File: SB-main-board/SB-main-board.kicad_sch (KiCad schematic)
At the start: 95 parts, among them J1 XT30PB_IN, J2 USB_C_Receptacle_USB2.0_16P, J3 Excluder, J4 PT100, J5 Hotend, J6 FAN2, J7 LDC, J8 FS, J9 FAN, Q1 BUK9M8R5-40EX, SW1 BOOT, U1 RP2040, U10 TMP235A2, U11 LP5912-3.3DRV, U2 W25Q16JVUXIQ, U3 TJA1042TK-3, U4 TPS54302, U5 LP5912-3.3DRV, U6 TMC2208-LA, U7 OR, U8 ADXL343, U9 MAX31865xTP, Y1 12MHz

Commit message: update to v2
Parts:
- removed C36: 1uF, Capacitor_SMD:C_0603_1608Metric, symbol Device:C_Small
- removed C37: 47pF, Capacitor_SMD:C_0402_1005Metric, symbol Device:C_Small
- removed FB1, FB2, FB3, FB4, FB6: 120R@100MHz, Inductor_SMD:L_0603_1608Metric, symbol Device:FerriteBead
- removed U11: LP5912-3.3DRV, Package_SON:WSON-6-1EP_2x2mm_P0.65mm_EP1x1.6mm, symbol Regulator_Linear:LP5912-3.3DRV
- removed U4: TPS54302, Package_TO_SOT_SMD:SOT-23-6, symbol Regulator_Switching:TPS565208
- removed U6: TMC2208-LA, Package_DFN_QFN:QFN-28-1EP_5x5mm_P0.5mm_EP3.75x3.75mm, symbol Driver_Motor:TMC2208-LA
- added D3: TPD4E02B04DQA, Package_SON:USON-10_2.5x1.0mm_P0.5mm, symbol Power_Protection:TPD4E02B04DQA
- added U4: TPS560430YF, Package_TO_SOT_SMD:SOT-23-6, symbol Library:TPS560430YF
- added U6: TMC2208-LA, Package_DFN_QFN:QFN-28-1EP_5x5mm_P0.5mm_EP3.75x3.75mm, symbol Library:TMC2208-LA
- C16: value 10uF -> 2.2uF
- C35: value 2.2uF -> 100nF; footprint Capacitor_SMD:C_0603_1608Metric -> Capacitor_SMD:C_0402_1005Metric
- D2: renamed from D3; value D_Schottky -> Schottky
- L1: footprint Inductor_SMD:L_Sunlord_SWPA4030S -> Library:L_Changjiang_FTC303020D
- R11: now fitted
- R12: value 100K -> 88.7K
- R13: value 13.3K -> 22.1K
- R7: footprint Resistor_SMD:R_0402_1005Metric -> Resistor_SMD:R_0805_2012Metric
- SW1: symbol Switch:SW_SPST -> Switch:SW_Push_Dual_x2
- U7: footprint Package_TO_SOT_SMD:SOT-23-5 -> Package_TO_SOT_SMD:SOT-353_SC-70-5
- renumbered C19 to C17, C17 to C18, C18 to C19, D2 to D4, FB5 to FB1
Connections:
- net +3V3B is gone; now on net +3V3: C20.1, C21.1, C29.1, C30.1, C31.1, C32.1, FB1.1, J8.4 (Pin_4), J9.8 (Pin_8), R14.1, U7.5 (VCC), U8.1 (Vdd_I/O), U8.6 (Vs), U9.19 (DVDD)
- net PGND is gone; now on net GND: C16.2, C18.2, C22.2, C23.2, C24.2, C27.2, C28.2, H1.1, H2.1, J1.2 (Pin_2), J3.MP (MountPin), J6.MP (MountPin), J7.MP (MountPin), J8.MP (MountPin), J9.10 (Pin_10), J9.12 (Pin_12), Q1.1 (S), Q1.2 (S), Q1.3 (S), R13.2, R15.2, R16.2, R20.2
- net +24V: now also C35.1, U4.5 (VIN), U6.22 (VS), U6.28 (VS)
- net +5V: no longer C35.1
- net ADC0: now also U1.39 (GPIO27_ADC1); no longer U1.38 (GPIO26_ADC0)
- net ADC1: now also U1.40 (GPIO28_ADC2); no longer U1.39 (GPIO27_ADC1)
- net ADXL_INT1: now also U1.3 (GPIO1); no longer U1.17 (GPIO14)
- net ADXL_INT2: now also U1.2 (GPIO0); no longer U1.18 (GPIO15)
- net CAN_RX: now also U1.30 (GPIO19); no longer U1.32 (GPIO21)
- net CAN_TX: now also U1.31 (GPIO20); no longer U1.34 (GPIO22)
- net ENDSTOP0: now also J8.2 (Pin_2); no longer J8.3 (Pin_3)
- net FAN0_PWM: now also U1.15 (GPIO12); no longer U1.11 (GPIO8)
- net FAN1_DET: now also U1.16 (GPIO13); no longer U1.9 (GPIO7)
- net FAN1_PWM: now also U1.14 (GPIO11); no longer U1.12 (GPIO9)
- net FAN2_DET: now also U1.18 (GPIO15); no longer U1.3 (GPIO1)
- net FAN2_PWM: now also U1.17 (GPIO14); no longer U1.2 (GPIO0)
- net FS: now also J8.3 (Pin_3), U1.38 (GPIO26_ADC0); no longer J8.2 (Pin_2), U1.40 (GPIO28_ADC2)
- net GND: now also D3.3 (G), D3.8 (G), U4.2 (GND), U6.10 (MS2), U6.13 (CLK), U6.18 (GND), U6.29 (EPAD), U6.3 (GND), U6.9 (MS1)
- net LDC_SCL: now also U1.9 (GPIO7); no longer U1.7 (GPIO5)
- net LDC_SDA: now also U1.11 (GPIO8); no longer U1.6 (GPIO4)
- net NEO: now also U1.12 (GPIO9); no longer U1.5 (GPIO3)
- net SPI0_CLK: now also U1.7 (GPIO5); no longer U1.16 (GPIO13)
- net SPI0_CS2: now also U1.6 (GPIO4); no longer U1.8 (GPIO6)
- net SPI0_MISO: now also U1.5 (GPIO3); no longer U1.15 (GPIO12)
- net SPI0_MOSI: now also U1.8 (GPIO6); no longer U1.14 (GPIO11)
- net TMC_DIAG: now also U6.11 (DIAG)
- net TMC_DIR: now also U1.32 (GPIO21), U6.19 (DIR); no longer U1.31 (GPIO20)
- net TMC_EN: now also U1.34 (GPIO22), U6.2 (ENN); no longer U1.30 (GPIO19)
- net TMC_STEP: now also U6.16 (STEP)
- net TMC_UART: now also U6.14 (PDN_UART)
- net USB_D+: now also D3.5 (IO4)
- net USB_D-: now also D3.4 (IO3)
- net at S1.3 (Pin_3), U9.5 (FORCE+): now also J4.1 (Pin_1); no longer J4.4 (Pin_4)
- net at C33.1, U9.7 (RTDIN+): now also J4.2 (Pin_2); no longer J4.3 (Pin_3)
- net at C33.2, U9.8 (RTDIN-): now also J4.3 (Pin_3); no longer J4.2 (Pin_2)
- net at U9.9 (FORCE-): now also J4.4 (Pin_4); no longer J4.1 (Pin_1)
- net at C25.1: now also U6.5 (CPI)
- net at C25.2: now also U6.4 (CPO)
- net at C15.1: now also U4.1 (BOOST)
- net at C15.2, L1.1: now also U4.6 (SW)
- net at C28.1, R16.1: now also U6.27 (BRB)
- net at R12.1, R13.1: now also U4.3 (FB)
- net at C27.1, R15.1: now also U6.23 (BRA)
- net at C26.1: now also U6.8 (5VOUT)
- net at C20.2: now also U6.6 (VCP)
- net at R11.2: now also U4.4 (EN)
- net at J3.1 (Pin_1): now also U6.1 (OB2)
- net at J3.4 (Pin_4): now also U6.21 (OA2)
- net at J3.3 (Pin_3): now also U6.24 (OA1)
- net at J3.2 (Pin_2): now also U6.26 (OB1)
- net +3V3A renamed +3V3
- net +3V3: now also U6.15 (VCC_IO)
- no-connect marks 11 -> 12
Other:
- moved on the sheet: C15, C16, C17, C18, C19, D2, J1, J2, J4, L1, R12, R13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

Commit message: sch: change accelerometer to LIS2DW12
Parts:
- removed U8: ADXL343, Package_LGA:LGA-14_3x5mm_P0.8mm_LayoutBorder1x6y, symbol Sensor_Motion:ADXL343
- added U8: LIS2DW12, Package_LGA:LGA-12_2x2mm_P0.5mm, symbol Library:LIS2DW12
- SW1: footprint Button_Switch_SMD:Panasonic_EVQPUJ_EVQPUA -> Library:Panasonic_EVQPUJ_EVQPUA
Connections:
- net +3V3: now also U8.10 (VDD_IO), U8.9 (VDD)
- net ADXL_INT1: now also U1.2 (GPIO0), U8.11 (INT2); no longer U1.3 (GPIO1)
- net ADXL_INT2: now also U1.3 (GPIO1), U8.12 (INT1); no longer U1.2 (GPIO0)
- net GND: now also U8.6 (GND), U8.7 (RES), U8.8 (GND)
- net SPI0_CLK: now also U8.1 (SCL)
- net SPI0_CS1: now also U8.2 (~{CS})
- net SPI0_MISO: now also U8.3 (SDO)
- net USB_D+: now also D3.6 (NC)
- net USB_D-: now also D3.7 (NC)
- net at U7.4: now also U8.4 (SDA)
- no-connect marks 12 -> 11
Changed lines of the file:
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@@
 	)
 	(junction
+		(at 214.63 152.4)
+		(diameter 0)
+		(color 0 0 0 0)
+	)
+	(junction
 		(at 31.75 109.22)
 		(diameter 0)
@@
 	)
 	(junction
+		(at 57.15 223.52)
+		(diameter 0)
+		(color 0 0 0 0)
+	)
+	(junction
 		(at 109.22 199.39)
 		(diameter 0)
@@
 	)
 	(junction
+		(at 62.23 223.52)
+		(diameter 0)
+		(color 0 0 0 0)
+	)
+	(junction
 		(at 102.87 118.11)
 		(diameter 0)
@@
 	)
 	(no_connect
-		(at 219.71 151.13)
-	)
-	(no_connect
 		(at 209.55 125.73)
 	)
@@
 	(wire
 		(pts
+			(xy 57.15 223.52) (xy 57.15 224.79)
+		)
+		(stroke
+			(width 0)
+			(type default)
+		)
+	)
+	(wire
+		(pts
 			(xy 191.77 135.89) (xy 201.93 135.89)
 		)
@@
 	(wire
 		(pts
+			(xy 59.69 223.52) (xy 62.23 223.52)
+		)
+		(stroke
+			(width 0)
+			(type default)
+		)
+	)
+	(wire
+		(pts
 			(xy 60.96 45.72) (xy 60.96 46.99)
 		)
@@
 		)
 	)
+	(wire
+		(pts
+			(xy 57.15 212.09) (xy 57.15 223.52)
+		)
+		(stroke
+			(width 0)
+			(type default)
+		)
+	)
 	(polyline
 		(pts
@@
 	(wire
 		(pts
-			(xy 62.23 207.01) (xy 62.23 224.79)
-		)
-		(stroke
-			(width 0)
-			(type default)
-		)
-	)
-	(wire
-		(pts
 			(xy 128.27 81.28) (xy 138.43 81.28)
 		)
@@
 	(wire
 		(pts
+			(xy 219.71 152.4) (xy 214.63 152.4)
+		)
+		(stroke
+			(width 0)
+			(type default)
+		)
+	)
+	(wire
+		(pts
 			(xy 72.39 261.62) (xy 77.47 261.62)
 		)
@@
 	(wire
 		(pts
+			(xy 54.61 223.52) (xy 57.15 223.52)
+		)
+		(stroke
+			(width 0)
+			(type default)
+		)
+	)
+	(wire
+		(pts
 			(xy 46.99 207.01) (xy 62.23 207.01)
 		)
@@
 	(wire
 		(pts
+			(xy 219.71 151.13) (xy 219.71 152.4)
+		)
+		(stroke
+			(width 0)
+			(type default)
+		)
+	)
+	(wire
+		(pts
 			(xy 97.79 24.13) (xy 97.79 25.4)
 		)
@@
 	(wire
 		(pts
+			(xy 62.23 223.52) (xy 62.23 224.79)
+		)
+		(stroke
+			(width 0)
+			(type default)
+		)
+	)
+	(wire
+		(pts
 			(xy 85.09 259.08) (xy 90.17 259.08)
 		)
@@
 	(wire
 		(pts
+			(xy 214.63 152.4) (xy 214.63 153.67)
+		)
+		(stroke
+			(width 0)
+			(type default)
+		)
+	)
+	(wire
+		(pts
 			(xy 262.89 151.13) (xy 266.7 151.13)
 		)
@@
 	(wire
 		(pts
-			(xy 57.15 212.09) (xy 57.15 224.79)
-		)
-		(stroke
-			(width 0)
-			(type default)
-		)
-	)
-	(wire
-		(pts
 			(xy 222.25 60.96) (xy 222.25 59.69)
 		)
@@
 	(wire
 		(pts
+			(xy 54.61 224.79) (xy 54.61 223.52)
+		)
+		(stroke
+			(width 0)
+			(type default)
+		)
+	)
+	(wire
+		(pts
 			(xy 128.27 88.9) (xy 138.43 88.9)
 		)
@@
 	(wire
 		(pts
+			(xy 62.23 207.01) (xy 62.23 223.52)
+		)
+		(stroke
+			(width 0)
+			(type default)
+		)
+	)
+	(wire
+		(pts
 			(xy 128.27 76.2) (xy 138.43 76.2)
 		)
@@
 	(wire
 		(pts
+			(xy 59.69 224.79) (xy 59.69 223.52)
+		)
+		(stroke
+			(width 0)
+			(type default)
+		)
+	)
+	(wire
+		(pts
 			(xy 44.45 45.72) (xy 48.26 45.72)
 		)
@@
 	)
 	(label "ADXL_INT1"
-		(at 138.43 35.56 180)
+		(at 138.43 33.02 180)
 		(fields_autoplaced yes)
 		(effects
@@
 	)
 	(label "ADXL_INT2"
-		(at 138.43 33.02 180)
+		(at 138.43 35.56 180)
 		(fields_autoplaced yes)
 		(effects
@@
 	)
 	(symbol
-		(lib_id "Sensor_Motion:ADXL343")
-		(at 214.63 138.43 0)
-		(unit 1)
-		(exclude_from_sim no)
-		(in_bom yes)
-		(on_board yes)
-		(dnp no)
-		(fields_autoplaced yes)
-		(property "Reference" "U8"
-			(at 229.87 132.1114 0)
-			(effects
-				(font
-					(size 1.27 1.27)
-				)
-			)
-		)
-		(property "Value" "ADXL343"
-			(at 229.87 134.6514 0)
-			(effects
-				(font
-					(size 1.27 1.27)
-				)
-			)
-		)
-		(property "Footprint" "Package_LGA:LGA-14_3x5mm_P0.8mm_LayoutBorder1x6y"
-			(at 214.63 138.43 0)
-			(effects
-				(font
-					(size 1.27 1.27)
-				)
-				(hide yes)
-			)
-		)
-		(property "Datasheet" "https://www.analog.com/media/en/technical-documentation/data-sheets/ADXL343.pdf"
-			(at 214.63 138.43 0)
-			(effects
-				(font
-					(size 1.27 1.27)
-				)
-				(hide yes)
-			)
-		)
-		(property "Description" "3-Axis MEMS Accelerometer, 2/4/8/16g range, I2C/SPI, LGA-14"
-			(at 214.63 138.43 0)
-			(effects
-				(font
-					(size 1.27 1.27)
-				)
-				(hide yes)
-			)
-		)
-		(pin "12"
-		)
-		(pin "13"
-		)
-		(pin "14"
-		)
-		(pin "5"
-		)
-		(pin "4"
-		)
-		(pin "11"
-		)
-		(pin "9"
-		)
-		(pin "3"
-		)
-		(pin "1"
-		)
-		(pin "8"
-		)
-		(pin "10"
-		)
-		(pin "2"
-		)
-		(pin "7"
-		)
-		(pin "6"
-		)
-		(instances
-			(project "SB-main-board"
-				(path "/e3d9bf3f-f8be-4a0d-9b69-f1016d65a8ba"
-					(reference "U8")
-					(unit 1)
-				)
-			)
-		)
-	)
-	(symbol
 		(lib_id "power:GND")
 		(at 87.63 137.16 0)
@@
 	(symbol
 		(lib_id "power:GND")
-		(at 214.63 152.4 0)
+		(at 214.63 153.67 0)
 		(unit 1)
 		(exclude_from_sim no)
@@
 		(fields_autoplaced yes)
 		(property "Reference" "#PWR0106"
-			(at 214.63 158.75 0)
+			(at 214.63 160.02 0)
 			(effects
 				(font
@@
 		)
 		(property "Value" "GND"
-			(at 214.63 157.48 0)
+			(at 214.63 158.75 0)
 			(effects
 				(font
@@
 		)
 		(property "Footprint" ""
-			(at 214.63 152.4 0)
+			(at 214.63 153.67 0)
 			(effects
 				(font
@@
 		)
 		(property "Datasheet" ""
-			(at 214.63 152.4 0)
+			(at 214.63 153.67 0)
 			(effects
 				(font
@@
 		)
 		(property "Description" "Power symbol creates a global label with name \"GND\" , ground"
-			(at 214.63 152.4 0)
+			(at 214.63 153.67 0)
 			(effects
 				(font
@@
 			)
 		)
-		(property "Footprint" "Button_Switch_SMD:Panasonic_EVQPUJ_EVQPUA"
+		(property "Footprint" "Library:Panasonic_EVQPUJ_EVQPUA"
 			(at 53.34 40.64 0)
 			(effects
@@
 					(unit 1)
 				)
+			)
+		)
+	)
+	(symbol
+		(lib_id "Library:LIS2DW12")
+		(at 214.63 138.43 0)
+		(unit 1)
+		(exclude_from_sim no)
+		(in_bom yes)
+		(on_board yes)
+		(dnp no)
+		(property "Reference" "U8"
+			(at 226.06 129.54 0)
+			(effects
+				(font
+					(size 1.27 1.27)
+				)
+				(justify left)
+			)
+		)
+		(property "Value" "LIS2DW12"
+			(at 226.06 132.08 0)
+			(effects
+				(font
+					(size 1.27 1.27)
+				)
+				(justify left)
+			)
+		)
+		(property "Footprint" "Package_LGA:LGA-12_2x2mm_P0.5mm"
+			(at 214.63 138.43 0)
+			(effects
+				(font
+					(size 1.27 1.27)
+				)
+				(hide yes)
+			)
+		)
+		(property "Datasheet" ""
+			(at 214.63 138.43 0)
+			(effects
+				(font
+					(size 1.27 1.27)
+				)
+				(hide yes)
+			)
+		)
+		(property "Description" "3-Axis MEMS Accelerometer, 2/4/8/16g range, I2C/SPI, LGA-12"
+			(at 214.63 138.43 0)
+			(effects
+				(font
+					(size 1.27 1.27)
+				)
+				(hide yes)
+			)
+		)
+		(pin "1"
+			(alternate "SPC")
+		)
+		(pin "5"
+		)
+		(pin "6"
+		)
+		(pin "10"
+		)
+		(pin "3"
+		)
+		(pin "2"
+		)
+		(pin "4"
+			(alternate "SDI")
+		)
+		(pin "12"
+		)
+		(pin "7"
+		)
+		(pin "11"
+		)
+		(pin "9"
+		)
+		(pin "8"
+		)
+		(instances
+			(project ""
+				(path "/e3d9bf3f-f8be-4a0d-9b69-f1016d65a8ba"
+					(reference "U8")
+					(unit 1)
+				)

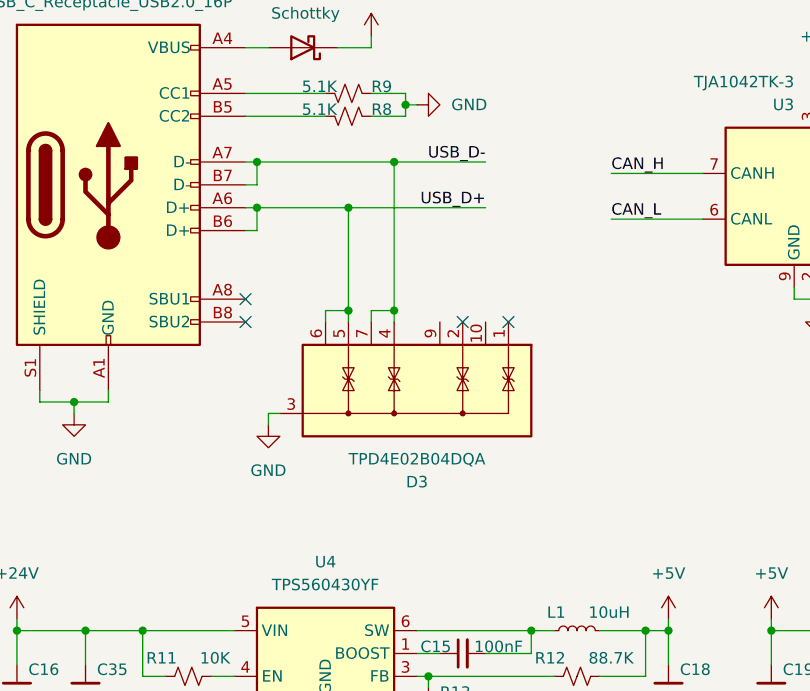
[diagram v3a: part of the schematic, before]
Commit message: sch: change the tvs to 0522
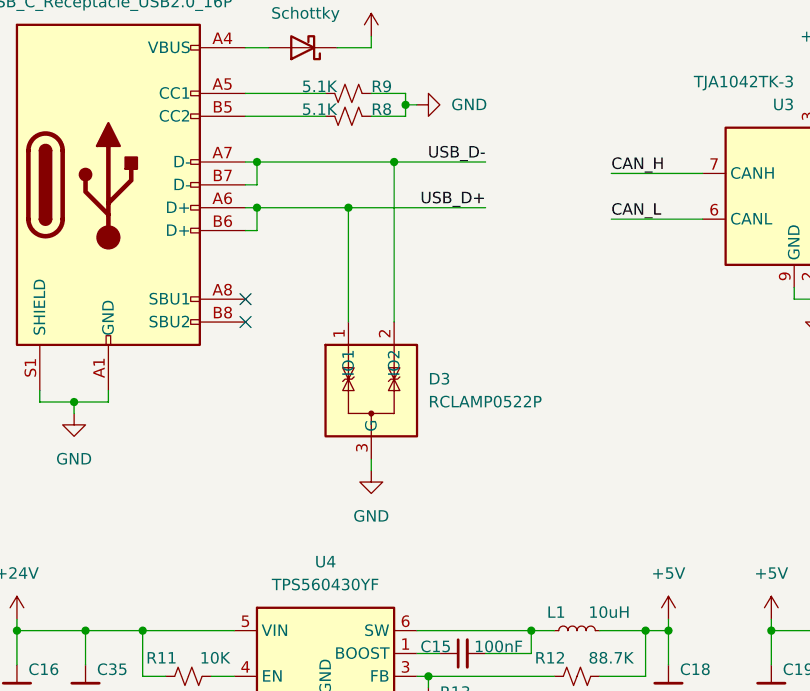
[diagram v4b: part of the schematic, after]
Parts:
- removed D3: TPD4E02B04DQA, Package_SON:USON-10_2.5x1.0mm_P0.5mm, symbol Power_Protection:TPD4E02B04DQA
- added D3: RCLAMP0522P, Library:SLP1610P4, symbol Library:RCLAMP0522P
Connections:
- net GND: now also D3.3 (G), D3.4 (G)
- net USB_D+: now also D3.1 (IO1), D3.6 (NC)
- net USB_D-: now also D3.2 (IO2), D3.5 (NC)
- no-connect marks 11 -> 9
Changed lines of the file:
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@@
 	)
 	(junction
-		(at 57.15 223.52)
-		(diameter 0)
-		(color 0 0 0 0)
-	)
-	(junction
 		(at 109.22 199.39)
 		(diameter 0)
@@
 	)
 	(junction
-		(at 62.23 223.52)
-		(diameter 0)
-		(color 0 0 0 0)
-	)
-	(junction
 		(at 102.87 118.11)
 		(diameter 0)
@@
 	)
 	(no_connect
-		(at 74.93 224.79)
-	)
-	(no_connect
 		(at 45.72 222.25)
 	)
@@
 	)
 	(no_connect
-		(at 69.85 224.79)
-	)
-	(no_connect
 		(at 45.72 224.79)
 	)
@@
 	(wire
 		(pts
+			(xy 57.15 212.09) (xy 57.15 224.79)
+		)
+		(stroke
+			(width 0)
+			(type default)
+		)
+	)
+	(wire
+		(pts
 			(xy 167.64 44.45) (xy 173.99 44.45)
 		)
@@
 	(wire
 		(pts
-			(xy 194.31 252.73) (xy 194.31 254)
+			(xy 59.69 240.03) (xy 59.69 241.3)
 		)
 		(stroke
@@
 	(wire
 		(pts
-			(xy 208.28 25.4) (xy 208.28 26.67)
+			(xy 194.31 252.73) (xy 194.31 254)
 		)
 		(stroke
@@
 		)
 	)
-	(polyline
+	(wire
 		(pts
-			(xy 240.03 233.68) (xy 240.03 163.83)
+			(xy 208.28 25.4) (xy 208.28 26.67)
 		)
 		(stroke
@@
 		)
 	)
-	(wire
+	(polyline
 		(pts
-			(xy 57.15 223.52) (xy 57.15 224.79)
+			(xy 240.03 233.68) (xy 240.03 163.83)
 		)
 		(stroke
@@
 	(wire
 		(pts
-			(xy 59.69 223.52) (xy 62.23 223.52)
-		)
-		(stroke
-			(width 0)
-			(type default)
-		)
-	)
-	(wire
-		(pts
 			(xy 60.96 45.72) (xy 60.96 46.99)
 		)
@@
 	(wire
 		(pts
+			(xy 62.23 207.01) (xy 62.23 224.79)
+		)
+		(stroke
+			(width 0)
+			(type default)
+		)
+	)
+	(wire
+		(pts
 			(xy 78.74 154.94) (xy 87.63 154.94)
 		)
@@
 		)
 	)
-	(wire
-		(pts
-			(xy 57.15 212.09) (xy 57.15 223.52)
-		)
-		(stroke
-			(width 0)
-			(type default)
-		)
-	)
 	(polyline
 		(pts
@@
 	(wire
 		(pts
-			(xy 48.26 234.95) (xy 49.53 234.95)
-		)
-		(stroke
-			(width 0)
-			(type default)
-		)
-	)
-	(wire
-		(pts
 			(xy 193.04 25.4) (xy 200.66 25.4)
 		)
@@
 	(wire
 		(pts
-			(xy 54.61 223.52) (xy 57.15 223.52)
-		)
-		(stroke
-			(width 0)
-			(type default)
-		)
-	)
-	(wire
-		(pts
 			(xy 46.99 207.01) (xy 62.23 207.01)
 		)
@@
 	(wire
 		(pts
-			(xy 62.23 223.52) (xy 62.23 224.79)
-		)
-		(stroke
-			(width 0)
-			(type default)
-		)
-	)
-	(wire
-		(pts
 			(xy 85.09 259.08) (xy 90.17 259.08)
 		)
@@
 	(wire
 		(pts
-			(xy 48.26 234.95) (xy 48.26 236.22)
-		)
-		(stroke
-			(width 0)
-			(type default)
-		)
-	)
-	(wire
-		(pts
 			(xy 120.65 154.94) (xy 129.54 154.94)
 		)
@@
 	(wire
 		(pts
-			(xy 54.61 224.79) (xy 54.61 223.52)
-		)
-		(stroke
-			(width 0)
-			(type default)
-		)
-	)
-	(wire
-		(pts
 			(xy 128.27 88.9) (xy 138.43 88.9)
 		)
@@
 	(wire
 		(pts
-			(xy 62.23 207.01) (xy 62.23 223.52)
-		)
-		(stroke
-			(width 0)
-			(type default)
-		)
-	)
-	(wire
-		(pts
 			(xy 128.27 76.2) (xy 138.43 76.2)
 		)
@@
 	(wire
 		(pts
-			(xy 59.69 224.79) (xy 59.69 223.52)
-		)
-		(stroke
-			(width 0)
-			(type default)
-		)
-	)
-	(wire
-		(pts
 			(xy 44.45 45.72) (xy 48.26 45.72)
 		)
@@
 	)
 	(symbol
+		(lib_id "Library:RCLAMP0522P")
+		(at 59.69 232.41 90)
+		(mirror x)
+		(unit 1)
+		(exclude_from_sim no)
+		(in_bom yes)
+		(on_board yes)
+		(dnp no)
+		(property "Reference" "D3"
+			(at 66.04 231.14 90)
+			(effects
+				(font
+					(size 1.27 1.27)
+				)
+				(justify right)
+			)
+		)
+		(property "Value" "RCLAMP0522P"
+			(at 66.04 233.68 90)
+			(effects
+				(font
+					(size 1.27 1.27)
+				)
+				(justify right)
+			)
+		)
+		(property "Footprint" "Library:SLP1610P4"
+			(at 67.31 232.41 0)
+			(effects
+				(font
+					(size 1.27 1.27)
+				)
+				(hide yes)
+			)
+		)
+		(property "Datasheet" ""
+			(at 67.31 232.41 0)
+			(effects
+				(font
+					(size 1.27 1.27)
+				)
+				(hide yes)
+			)
+		)
+		(property "Description" ""
+			(at 67.31 232.41 0)
+			(effects
+				(font
+					(size 1.27 1.27)
+				)
+				(hide yes)
+			)
+		)
+		(pin "1"
+		)
+		(pin "2"
+		)
+		(pin "6"
+		)
+		(pin "4"
+		)
+		(pin "3"
+		)
+		(pin "5"
+		)
+		(instances
+			(project ""
+				(path "/e3d9bf3f-f8be-4a0d-9b69-f1016d65a8ba"
+					(reference "D3")
+					(unit 1)
+				)
+			)
+		)
+	)
+	(symbol
 		(lib_id "Device:C_Small")
 		(at 87.63 151.13 0)
@@
 	(symbol
 		(lib_id "power:GND")
-		(at 48.26 236.22 0)
+		(at 59.69 241.3 0)
 		(unit 1)
 		(exclude_from_sim no)
@@
 		(fields_autoplaced yes)
 		(property "Reference" "#PWR07"
-			(at 48.26 242.57 0)
+			(at 59.69 247.65 0)
 			(effects
 				(font
@@
 		)
 		(property "Value" "GND"
-			(at 48.26 241.3 0)
+			(at 59.69 246.38 0)
 			(effects
 				(font
@@
 		)
 		(property "Footprint" ""
-			(at 48.26 236.22 0)
+			(at 59.69 241.3 0)
 			(effects
 				(font
@@
 		)
 		(property "Datasheet" ""
-			(at 48.26 236.22 0)
+			(at 59.69 241.3 0)
 			(effects
 				(font
@@
 		)
 		(property "Description" ""
-			(at 48.26 236.22 0)
+			(at 59.69 241.3 0)
 			(effects
 				(font
@@
 					(unit 1)
 				)
-			)
-		)
-	)
-	(symbol
-		(lib_id "Power_Protection:TPD4E02B04DQA")
-		(at 64.77 232.41 270)
-		(unit 1)
-		(exclude_from_sim no)
-		(in_bom yes)
-		(on_board yes)
-		(dnp no)
-		(property "Reference" "D3"
-			(at 64.77 242.57 90)
-			(effects
-				(font
-					(size 1.27 1.27)
-				)
-			)
-		)
-		(property "Value" "TPD4E02B04DQA"
-			(at 64.77 240.03 90)
-			(effects
-				(font
-					(size 1.27 1.27)
-				)
-			)
-		)
-		(property "Footprint" "Package_SON:USON-10_2.5x1.0mm_P0.5mm"
-			(at 64.77 240.03 0)
-			(effects
-				(font
-					(size 1.27 1.27)
-				)
-				(justify left)
-				(hide yes)
-			)
-		)
-		(property "Datasheet" "http://www.ti.com/lit/ds/symlink/tpd4e02b04.pdf"
-			(at 64.77 234.95 0)
-			(effects
-				(font
-					(size 1.27 1.27)
-				)
-				(hide yes)
-			)
-		)
-		(property "Description" "4-Channel ESD Protection Diode for USB Type-C and HDMI 2.0, USON-10"
-			(at 64.77 232.41 0)
-			(effects
-				(font
-					(size 1.27 1.27)
-				)
-				(hide yes)
-			)
-		)
-		(pin "9"
-		)
-		(pin "2"
-		)
-		(pin "8"
-		)
-		(pin "1"
-		)
-		(pin "10"
-		)
-		(pin "7"
-		)
-		(pin "4"
-		)
-		(pin "3"
-		)
-		(pin "6"
-		)
-		(pin "5"
-		)
-		(instances
-			(project "SB-main-board"
-				(path "/e3d9bf3f-f8be-4a0d-9b69-f1016d65a8ba"
-					(reference "D3")
-					(unit 1)
-				)
